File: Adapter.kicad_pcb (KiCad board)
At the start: 6 copper layers, 189.7 x 92 mm, 291 parts, among them J1 GD820HTX75P6HB, J2 2-338069-0, U1 R-78E3.3-1.0, U10 74LVC1G04, U11 LMV7219M5, U2 LM1117GS-3.3, U4 74LVC1G04, U5 ADuM1200AR, U6 74LVC1G04, U7 74LVC1G04, U8 74LVC1G04, U9 74LVC1G04

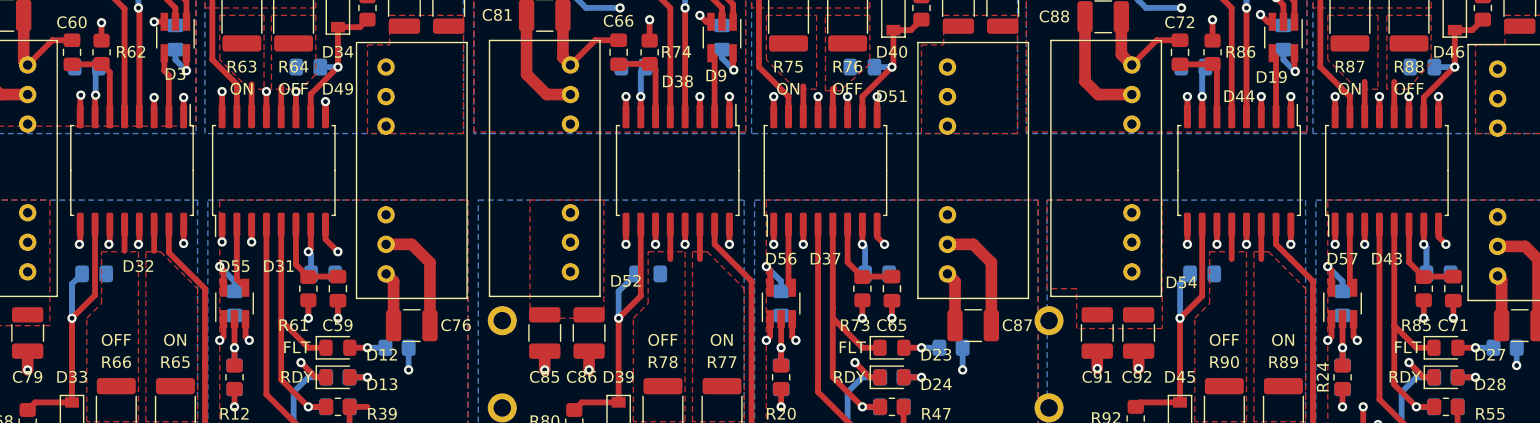
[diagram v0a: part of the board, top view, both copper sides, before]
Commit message: Поменял драйвера на китайские
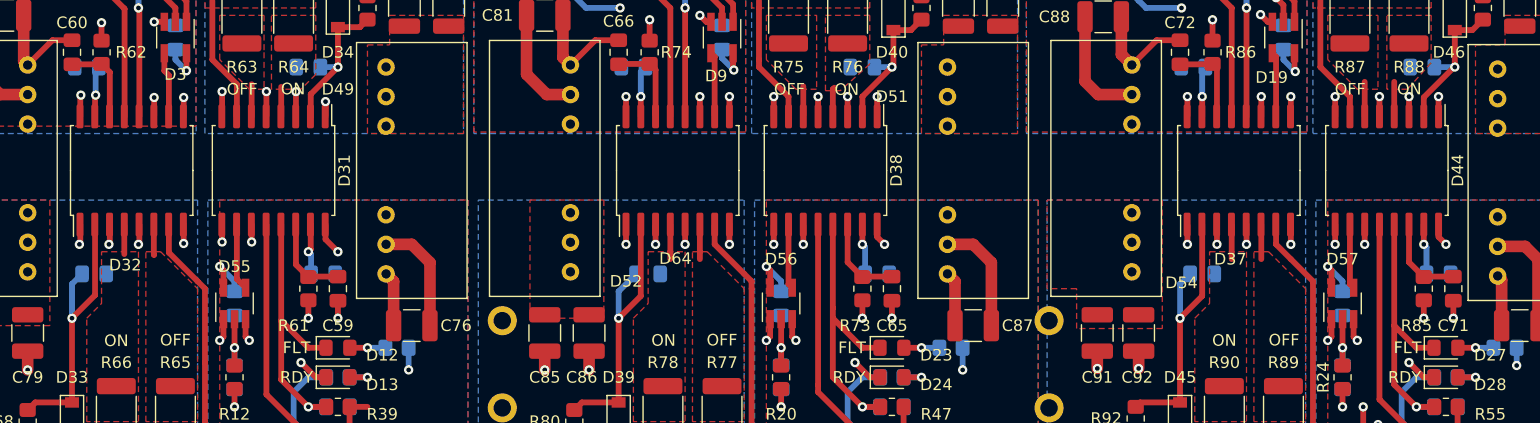
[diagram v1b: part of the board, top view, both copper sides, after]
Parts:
- removed D43: ADUM4135, Package_SO:SOIC-16W_7.5x10.3mm_P1.27mm
- added D64: NSI6651, Package_SO:SOIC-16W_7.5x10.3mm_P1.27mm, F.Cu at (138.4, 91.4)
- D31, D32, D37, D38, D44: value ADUM4135 -> NSI6651
- moved D37 35.5 mm to (186.7, 91.4)
- moved D38 12.7 mm to (151.1, 91.4)
- moved D44 12.7 mm to (199.4, 91.4)
- turned D32 to 90 degrees
- turned D31 to -90 degrees
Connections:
- C59 pad 2: Net-(D31-~{RESET}) -> Net-(D31-~{RST})
- C60 pad 2: Net-(D32-~{RESET}) -> Net-(D32-~{RST})
- C65 pad 2: Net-(D37-~{RESET}) -> Net-(D38-~{RST})
- C66 pad 2: Net-(D38-~{RESET}) -> Net-(D64-~{RST})
- C67 pad 1: Net-(D38-DESAT) -> Net-(D39-K)
- C68 pad 1: Net-(D37-DESAT) -> Net-(D38-DESAT)
- C71 pad 2: Net-(D43-~{RESET}) -> Net-(D44-~{RST})
- C72 pad 2: Net-(D44-~{RESET}) -> Net-(D37-~{RST})
- C73 pad 1: Net-(D44-DESAT) -> Net-(D37-DESAT)
- C74 pad 1: Net-(D43-DESAT) -> Net-(D44-DESAT)
- D31 pad 1: GND -> -15V_L1
- D31 pad 10: Net-(D31-DESAT) -> PWM_L1
- D31 pad 11: E2 -> GND
- D31 pad 12: Net-(D31-Vout_off) -> RDY_L1
- D31 pad 13: +15V_L1 -> FLT_L1
- D31 pad 14: Net-(D31-Vout_on) -> Net-(D31-~{RST})
- D31 pad 15: G2 -> +3V3
- D31 pad 16: -15V_L1 -> GND
- D31 pad 2: PWM_L1 -> Net-(D31-DESAT)
- D31 pad 3: GND -> E2
- D31 pad 4: RDY_L1 -> Net-(D31-OUTH)
- D31 pad 5: FLT_L1 -> +15V_L1
- D31 pad 6: Net-(D31-~{RESET}) -> Net-(D31-OUTL)
- D31 pad 7: +3V3 -> G2
- D31 pad 8: GND -> -15V_L1
- D31 pad 9: -15V_L1 -> GND
- D32 pad 1: GND -> -15V_H1
- D32 pad 10: Net-(D32-DESAT) -> PWM_H1
- D32 pad 11: E1 -> GND
- D32 pad 12: Net-(D32-Vout_off) -> RDY_H1
- D32 pad 13: +15V_H1 -> FLT_H1
- D32 pad 14: Net-(D32-Vout_on) -> Net-(D32-~{RST})
- D32 pad 15: G1 -> +3V3
- D32 pad 16: -15V_H1 -> GND
- D32 pad 2: PWM_H1 -> Net-(D32-DESAT)
- D32 pad 3: GND -> E1
- D32 pad 4: RDY_H1 -> Net-(D32-OUTH)
- D32 pad 5: FLT_H1 -> +15V_H1
- D32 pad 6: Net-(D32-~{RESET}) -> Net-(D32-OUTL)
- D32 pad 7: +3V3 -> G1
- D32 pad 8: GND -> -15V_H1
- D32 pad 9: -15V_H1 -> GND
- D37 pad 1: GND -> -15V_H3
- D37 pad 10: Net-(D37-DESAT) -> PWM_H3
- D37 pad 11: E4 -> GND
- D37 pad 12: Net-(D37-Vout_off) -> RDY_H3
- D37 pad 13: +15V_L2 -> FLT_H3
- D37 pad 14: Net-(D37-Vout_on) -> Net-(D37-~{RST})
- D37 pad 15: G4 -> +3V3
- D37 pad 16: -15V_L2 -> GND
- D37 pad 2: PWM_L2 -> Net-(D37-DESAT)
- D37 pad 3: GND -> E5
- D37 pad 4: RDY_L2 -> Net-(D37-OUTH)
- D37 pad 5: FLT_L2 -> +15V_H3
- D37 pad 6: Net-(D37-~{RESET}) -> Net-(D37-OUTL)
- D37 pad 7: +3V3 -> G5
- D37 pad 8: GND -> -15V_H3
- D37 pad 9: -15V_L2 -> GND
- D38 pad 1: GND -> -15V_L2
- D38 pad 10: Net-(D38-DESAT) -> PWM_L2
- D38 pad 11: E3 -> GND
- D38 pad 12: Net-(D38-Vout_off) -> RDY_L2
- D38 pad 13: +15V_H2 -> FLT_L2
- D38 pad 14: Net-(D38-Vout_on) -> Net-(D38-~{RST})
- D38 pad 15: G3 -> +3V3
- D38 pad 16: -15V_H2 -> GND
- D38 pad 2: PWM_H2 -> Net-(D38-DESAT)
- D38 pad 3: GND -> E4
- D38 pad 4: RDY_H2 -> Net-(D38-OUTH)
- D38 pad 5: FLT_H2 -> +15V_L2
- D38 pad 6: Net-(D38-~{RESET}) -> Net-(D38-OUTL)
- D38 pad 7: +3V3 -> G4
- D38 pad 8: GND -> -15V_L2
- D38 pad 9: -15V_H2 -> GND
- D39 pad 1: Net-(D38-DESAT) -> Net-(D39-K)
- D40 pad 1: Net-(D37-DESAT) -> Net-(D38-DESAT)
- D44 pad 1: GND -> -15V_L3
- D44 pad 10: Net-(D44-DESAT) -> PWM_L3
- D44 pad 11: E5 -> GND
- D44 pad 12: Net-(D44-Vout_off) -> RDY_L3
- D44 pad 13: +15V_H3 -> FLT_L3
- D44 pad 14: Net-(D44-Vout_on) -> Net-(D44-~{RST})
- D44 pad 15: G5 -> +3V3
- D44 pad 16: -15V_H3 -> GND
- D44 pad 2: PWM_H3 -> Net-(D44-DESAT)
- D44 pad 3: GND -> E6
- D44 pad 4: RDY_H3 -> Net-(D44-OUTH)
- D44 pad 5: FLT_H3 -> +15V_L3
- D44 pad 6: Net-(D44-~{RESET}) -> Net-(D44-OUTL)
- D44 pad 7: +3V3 -> G6
- D44 pad 8: GND -> -15V_L3
- D44 pad 9: -15V_H3 -> GND
- D45 pad 1: Net-(D44-DESAT) -> Net-(D37-DESAT)
- D46 pad 1: Net-(D43-DESAT) -> Net-(D44-DESAT)
- R61 pad 2: Net-(D31-~{RESET}) -> Net-(D31-~{RST})
- R62 pad 2: Net-(D32-~{RESET}) -> Net-(D32-~{RST})
- R63 pad 2: Net-(D31-Vout_on) -> Net-(D31-OUTL)
- R64 pad 2: Net-(D31-Vout_off) -> Net-(D31-OUTH)
- R65 pad 2: Net-(D32-Vout_on) -> Net-(D32-OUTL)
- R66 pad 2: Net-(D32-Vout_off) -> Net-(D32-OUTH)
- R73 pad 2: Net-(D37-~{RESET}) -> Net-(D38-~{RST})
- R74 pad 2: Net-(D38-~{RESET}) -> Net-(D64-~{RST})
- R75 pad 2: Net-(D37-Vout_on) -> Net-(D38-OUTL)
- R76 pad 2: Net-(D37-Vout_off) -> Net-(D38-OUTH)
- R77 pad 2: Net-(D38-Vout_on) -> Net-(D64-OUTL)
- R78 pad 2: Net-(D38-Vout_off) -> Net-(D64-OUTH)
- R79 pad 2: Net-(D37-DESAT) -> Net-(D38-DESAT)
- R80 pad 2: Net-(D38-DESAT) -> Net-(D39-K)
- R85 pad 2: Net-(D43-~{RESET}) -> Net-(D44-~{RST})
- R86 pad 2: Net-(D44-~{RESET}) -> Net-(D37-~{RST})
- R87 pad 2: Net-(D43-Vout_on) -> Net-(D44-OUTL)
- R88 pad 2: Net-(D43-Vout_off) -> Net-(D44-OUTH)
- R89 pad 2: Net-(D44-Vout_on) -> Net-(D37-OUTL)
- R90 pad 2: Net-(D44-Vout_off) -> Net-(D37-OUTH)
- R91 pad 2: Net-(D43-DESAT) -> Net-(D44-DESAT)
- R92 pad 2: Net-(D44-DESAT) -> Net-(D37-DESAT)
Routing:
- net Net-(D39-K): track 0.00 -> 24.6 mm, vias 0 -> 1
- net Net-(D43-DESAT): track 13.1 -> 0.00 mm, vias 1 -> 0
- net Net-(D38-DESAT): track 24.6 -> 12.8 mm
- net Net-(D37-DESAT): track 12.8 -> 24.2 mm
- net Net-(D44-DESAT): track 24.2 -> 13.1 mm
- net Net-(D44-~{RST}): track 0.00 -> 7.59 mm
- net Net-(D43-~{RESET}): track 7.59 -> 0.00 mm
- net Net-(D38-~{RST}): track 0.00 -> 7.59 mm
- net Net-(D37-~{RESET}): track 7.59 -> 0.00 mm
- net Net-(D31-~{RST}): track 0.00 -> 7.51 mm
- net Net-(D31-~{RESET}): track 7.51 -> 0.00 mm
- net Net-(D44-~{RESET}): track 7.48 -> 0.00 mm
- net Net-(D37-~{RST}): track 0.00 -> 7.48 mm
- net Net-(D64-~{RST}): track 0.00 -> 7.40 mm
- net Net-(D38-~{RESET}): track 7.40 -> 0.00 mm
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- added copper zone on F.Cu, net Net-(D31-OUTH)
- added copper zone on F.Cu, net Net-(D31-OUTL)
- added copper zone on F.Cu, net Net-(D32-OUTH)
- added copper zone on F.Cu, net Net-(D32-OUTL)
- added copper zone on F.Cu, net Net-(D37-OUTH)
- added copper zone on F.Cu, net Net-(D37-OUTL)
- added copper zone on F.Cu, net Net-(D38-OUTH)
- added copper zone on F.Cu, net Net-(D38-OUTL)
- added copper zone on F.Cu, net Net-(D44-OUTH)
- added copper zone on F.Cu, net Net-(D44-OUTL)
- added copper zone on F.Cu, net Net-(D64-OUTH)
- added copper zone on F.Cu, net Net-(D64-OUTL)
- removed copper zone on F.Cu, net Net-(D31-Vout_off)
- removed copper zone on F.Cu, net Net-(D31-Vout_on)
- removed copper zone on F.Cu, net Net-(D32-Vout_off)
- removed copper zone on F.Cu, net Net-(D32-Vout_on)
- removed copper zone on F.Cu, net Net-(D37-Vout_off)
- removed copper zone on F.Cu, net Net-(D37-Vout_on)
- removed copper zone on F.Cu, net Net-(D38-Vout_off)
- removed copper zone on F.Cu, net Net-(D38-Vout_on)
- removed copper zone on F.Cu, net Net-(D43-Vout_off)
- removed copper zone on F.Cu, net Net-(D43-Vout_on)
- removed copper zone on F.Cu, net Net-(D44-Vout_off)
- removed copper zone on F.Cu, net Net-(D44-Vout_on)
